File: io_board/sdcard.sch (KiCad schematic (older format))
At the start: 4 parts

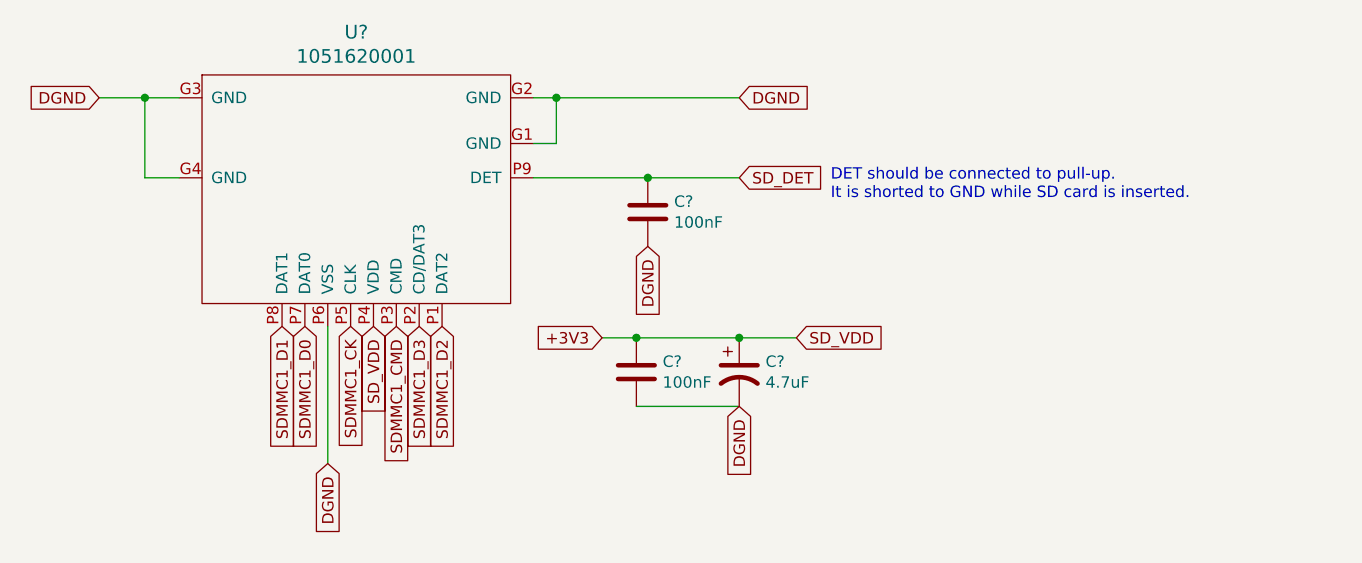
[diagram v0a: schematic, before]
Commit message: Added MIDI connectors and SD card to io_board
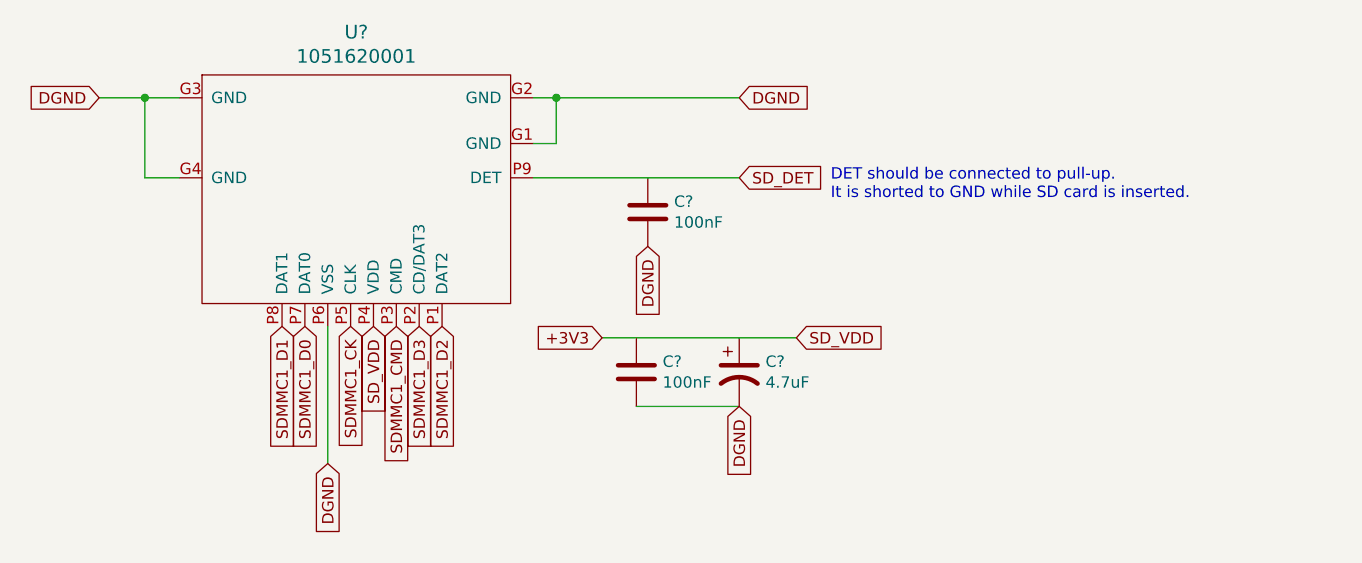
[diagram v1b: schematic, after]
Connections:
- net +3V3: no longer C?.1, C?.1
- net SD_DET: no longer C?.1
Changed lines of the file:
@@
 EESchema Schematic File Version 4
-LIBS:midi_studio_v1-cache
-EELAYER 26 0
+LIBS:io_board-cache
+EELAYER 29 0
 EELAYER END
 $Descr A4 11693 8268
 encoding utf-8
-Sheet 8 13
+Sheet 8 8
 Title ""
 Date ""
@@
 Text GLabel 6600 4350 0    50   Input ~ 0
 +3V3
-Wire Wire Line
-	6600 4350 6750 4350
 $Comp
 L Device:C C?
@@
 	1    0    0    -1
 $EndComp
-Connection ~ 7200 4350
-Wire Wire Line
-	7200 4350 7450 4350
-Connection ~ 6750 4350
-Wire Wire Line
-	6750 4350 7200 4350
-Wire Wire Line
-	6300 3650 6800 3650
 $Comp
 L Device:C C?
@@
 	1    0    0    -1
 $EndComp
-Connection ~ 6800 3650
-Wire Wire Line
-	6800 3650 7200 3650
 Wire Wire Line
 	6750 4650 7200 4650
@@
 Text GLabel 6800 3950 3    50   Input ~ 0
 DGND
+Wire Wire Line
+	6600 4350 7450 4350
+Wire Wire Line
+	6300 3650 7200 3650
 $EndSCHEMATC
